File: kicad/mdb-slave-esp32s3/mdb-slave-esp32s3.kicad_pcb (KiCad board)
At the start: 2 copper layers, 39 x 40 mm, 45 parts, among them J1 MDB_Connector, J2 USB_C_Receptacle_USB2.0_16P, J3 Conn_01x03_Pin, J8 Conn_01x04_Pin, Q7 MMBT3904, SW1 SW_Push, U1 TLP785, U3 ESP32-S3FH4R2, U4 TLP785, U5 LM2594HVM-3.3, Y1 Crystal_GND24

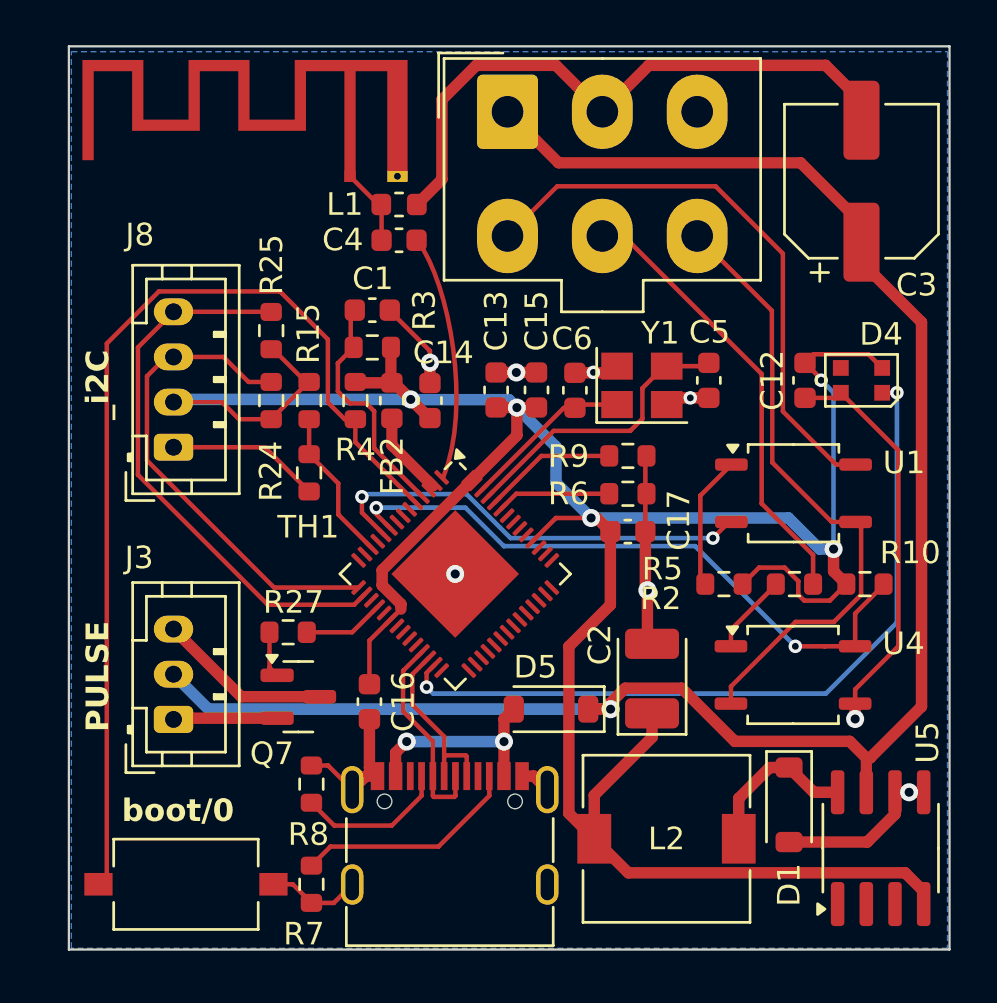
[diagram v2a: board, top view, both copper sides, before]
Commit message: small mounting hole
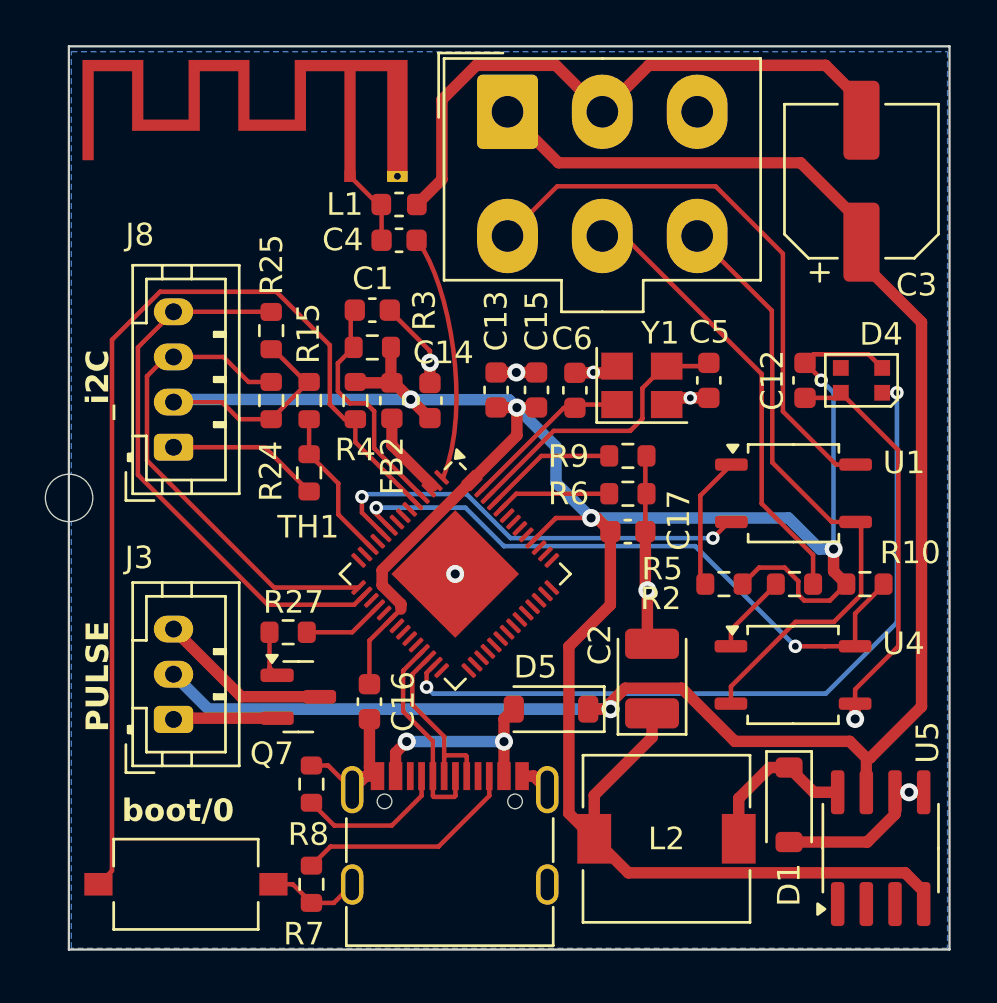
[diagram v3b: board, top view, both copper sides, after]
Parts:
- added H1: MountingHole, MountingHole:MountingHole_2.1mm, F.Cu at (168.5, 103.1)
- moved REF** 0.13 mm to (193.6, 107.4)

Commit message: routing pcb
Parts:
- moved C14 0.08 mm to (184.4, 98.8)
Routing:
- net GND: track 94.4 -> 82.0 mm, vias 8 -> 9
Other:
- board text added: "commit xxxxxxx"
- board text added: "i2C"
- board text removed: "_i2C"
- board text removed: "commit: xxxxxxx"

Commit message: routing...
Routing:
- net GND: track 82.0 -> 69.2 mm, vias 9 -> 10
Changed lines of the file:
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@@
 	(footprint "MountingHole:MountingHole_2.1mm"
 		(layer "F.Cu")
-		(at 168.51 103.09)
+		(at 168.5 103.09)
 		(descr "Mounting Hole 2.1mm, no annular, generated by kicad-footprint-generator mountinghole.py")
 		(tags "mountinghole")
@@
 	)
 	(segment
-		(start 185.02 88.9875)
-		(end 185.02 85.45837)
-		(width 0.508)
-		(layer "F.Cu")
-		(net 3)
-	)
-	(segment
 		(start 195.27 98.66)
 		(end 194.975 98.955)
@@
 	)
 	(segment
-		(start 185.02 85.45837)
-		(end 186.54577 83.9326)
-		(width 0.508)
-		(layer "F.Cu")
-		(net 3)
-	)
-	(segment
 		(start 202.46 98.66)
 		(end 202.685 98.435)
@@
 	)
 	(segment
+		(start 183.91 90.0975)
+		(end 184.79 90.0975)
+		(width 0.508)
+		(layer "F.Cu")
+		(net 3)
+	)
+	(segment
 		(start 205.085 117.099999)
 		(end 205.085 116.125)
@@
 	)
 	(segment
-		(start 190.0676 83.9326)
-		(end 192.125 85.99)
-		(width 0.508)
-		(layer "F.Cu")
-		(net 3)
-	)
-	(segment
 		(start 180.234 121.025)
 		(end 181.049 120.21)
@@
 	)
 	(segment
-		(start 186.54577 83.9326)
-		(end 190.0676 83.9326)
-		(width 0.508)
-		(layer "F.Cu")
-		(net 3)
-	)
-	(segment
 		(start 203.854999 118.33)
 		(end 205.085 117.099999)
@@
 	)
 	(segment
-		(start 183.91 90.0975)
-		(end 185.02 88.9875)
-		(width 0.508)
-		(layer "F.Cu")
-		(net 3)
-	)
-	(segment
 		(start 194.17 104.72)
 		(end 194.03 104.58)
@@
 		(net 3)
 	)
+	(via
+		(at 184.79 90.0975)
+		(size 0.8)
+		(drill 0.4)
+		(layers "F.Cu" "B.Cu")
+		(free yes)
+		(net 3)
+	)
 	(segment
 		(start 196.695 97.255)
@@
 	)
 	(segment
-		(start 173.135 110.898333)
-		(end 174.681667 112.445)
+		(start 183.925 112.445)
+		(end 192.49 112.445)
 		(width 0.508)
 		(layer "B.Cu")
@@
 	)
 	(segment
-		(start 174.681667 112.445)
-		(end 192.49 112.445)
+		(start 182.378333 110.898333)
+		(end 183.925 112.445)
+		(width 0.508)
+		(layer "B.Cu")
+		(net 7)
+	)
+	(segment
+		(start 173.135 110.898333)
+		(end 182.378333 110.898333)
 		(width 0.508)
 		(layer "B.Cu")
@@
 	(segment
 		(start 197.84 104.72)
-		(end 187.764308 104.72)
+		(end 190.9 104.72)
 		(width 0.2032)
 		(layer "B.Cu")
@@
 	)
 	(segment
-		(start 187.764308 104.72)
-		(end 186.012953 102.968645)
+		(start 190.9 104.72)
+		(end 189.148645 102.968645)
 		(width 0.2032)
 		(layer "B.Cu")
@@
 	)
 	(segment
-		(start 186.012953 102.968645)
+		(start 189.148645 102.968645)
 		(end 181.546914 102.968645)
 		(width 0.2032)
@@
 	)
 	(segment
-		(start 182.113272 103.523645)
-		(end 186.063645 103.523645)
+		(start 190.735 105.225)
+		(end 196.235 105.225)
 		(width 0.2032)
 		(layer "B.Cu")
@@
 	)
 	(segment
-		(start 187.765 105.225)
-		(end 196.235 105.225)
+		(start 196.235 105.225)
+		(end 200.671738 109.661738)
 		(width 0.2032)
 		(layer "B.Cu")
@@
 	)
 	(segment
-		(start 196.235 105.225)
-		(end 200.671738 109.661738)
+		(start 189.033645 103.523645)
+		(end 190.735 105.225)
 		(width 0.2032)
 		(layer "B.Cu")
@@
 	)
 	(segment
-		(start 186.063645 103.523645)
-		(end 187.765 105.225)
+		(start 182.113272 103.523645)
+		(end 189.033645 103.523645)
 		(width 0.2032)
 		(layer "B.Cu")
@@
 		(name "$teardrop_padvia$")
 		(hatch none 0.1)
-		(priority 30010)
+		(priority 30009)
 		(attr
 			(teardrop
@@
 	)
 	(zone
-		(net 23)
-		(net_name "/io10")
+		(net 2)
+		(net_name "+3V3")
 		(layer "F.Cu")
 		(name "$teardrop_padvia$")
 		(hatch none 0.1)
-		(priority 30005)
+		(priority 30007)
 		(attr
 			(teardrop
@@
 		(polygon
 			(pts
-				(xy 171.92558 97.592999) (xy 172.067001 97.73442) (xy 173.327746 97.446667) (xy 173.135707 96.84596)
-				(xy 172.271529 96.729613)
+				(xy 174.598471 98.946667) (xy 174.598471 98.746667) (xy 173.743342 98.347785) (xy 173.134 98.846667)
+				(xy 173.743342 99.345549)
 			)
 		)
@@
 		(name "$teardrop_padvia$")
 		(hatch none 0.1)
-		(priority 30003)
+		(priority 30002)
 		(attr
 			(teardrop
@@
 	)
 	(zone
-		(net 23)
-		(net_name "/io10")
+		(net 12)
+		(net_name "/mdb_master_receive")
 		(layer "F.Cu")
 		(name "$teardrop_padvia$")
 		(hatch none 0.1)
-		(priority 30009)
+		(priority 30001)
 		(attr
 			(teardrop
@@
 		(polygon
 			(pts
-				(xy 174.598471 96.946667) (xy 174.598471 96.746667) (xy 173.743342 96.347785) (xy 173.134 96.846667)
-				(xy 173.743342 97.345549)
+				(xy 189.792438 89.763983) (xy 189.651017 89.622562) (xy 188.139088 89.861698) (xy 187.924293 91.490707)
+				(xy 189.275 91.554214)
 			)
 		)
@@
 		(name "$teardrop_padvia$")
 		(hatch none 0.1)
-		(priority 30000)
+		(priority 30013)
 		(attr
 			(teardrop
@@
 		(polygon
 			(pts
-				(xy 190.507878 84.013668) (xy 190.148668 84.372878) (xy 190.775 86.054213) (xy 192.125707 85.990707)
-				(xy 191.910911 84.361698)
+				(xy 180.192157 120.9234) (xy 180.192157 121.1266) (xy 180.872955 121.067877) (xy 181.05 120.21)
+				(xy 180.549 119.996303)
 			)
 		)
 	)
 	(zone
-		(net 72)
-		(net_name "Net-(J3-Pin_3)")
+		(net 3)
+		(net_name "GND")
 		(layer "F.Cu")
 		(name "$teardrop_padvia$")
 		(hatch none 0.1)
-		(priority 30004)
+		(priority 30005)
 		(attr
 			(teardrop
@@
 		(polygon
 			(pts
-				(xy 173.9106 110.033144) (xy 174.269811 109.673933) (xy 173.998471 108.913276) (xy 173.134293 108.897626)
-				(xy 172.886472 109.498333)
+				(xy 174.61 100.948267) (xy 174.61 100.745067) (xy 173.855671 100.265697) (xy 173.134 100.846667)
+				(xy 173.855671 101.427637)
 			)
 		)
@@
 		(name "$teardrop_padvia$")
 		(hatch none 0.1)
-		(priority 30012)
+		(priority 30010)
 		(attr
 			(teardrop
@@
 		(polygon
 			(pts
-				(xy 188.730421 115.156) (xy 188.730421 115.664) (xy 189.189 116.286434) (xy 189.69 116.01) (xy 189.287099 115.16838)
+				(xy 182.007579 115.664) (xy 182.007579 115.156) (xy 181.4509 115.16838) (xy 181.048 116.01) (xy 181.549 116.286434)
 			)
 		)
 	)
 	(zone
-		(net 3)
-		(net_name "GND")
+		(net 23)
+		(net_name "/io10")
 		(layer "F.Cu")
 		(name "$teardrop_padvia$")
 		(hatch none 0.1)
-		(priority 30011)
+		(priority 30004)
 		(attr
 			(teardrop
@@
 		(polygon
 			(pts
-				(xy 182.007579 115.664) (xy 182.007579 115.156) (xy 181.4509 115.16838) (xy 181.048 116.01) (xy 181.549 116.286434)
+				(xy 171.92558 97.592999) (xy 172.067001 97.73442) (xy 173.327746 97.446667) (xy 173.135707 96.84596)
+				(xy 172.271529 96.729613)
 			)
 		)
@@
 		(name "$teardrop_padvia$")
 		(hatch none 0.1)
-		(priority 30007)
+		(priority 30006)
 		(attr
 			(teardrop
@@
 	)
 	(zone
-		(net 11)
-		(net_name "/mdb_communications_common")
-		(layer "F.Cu")
-		(name "$teardrop_padvia$")
-		(hatch none 0.1)
-		(priority 30001)
-		(attr
-			(teardrop
-				(type padvia)
-			)
-		)
-		(connect_pads yes
-			(clearance 0)
-		)
-		(min_thickness 0.0254)
-		(filled_areas_thickness no)
-		(fill yes
-			(thermal_gap 0.5)
-			(thermal_bridge_width 0.5)
-			(island_removal_mode 1)
-			(island_area_min 10)
-		)
-		(polygon
-			(pts
-				(xy 198.051017 93.357438) (xy 198.192438 93.216017) (xy 197.675 91.425786) (xy 196.324293 91.489293)
-				(xy 196.539087 93.118301)
-			)
-		)
-	)
-	(zone
 		(net 3)
 		(net_name "GND")
@@
 		(name "$teardrop_padvia$")
 		(hatch none 0.1)
-		(priority 30013)
+		(priority 30012)
 		(attr
 			(teardrop
@@
 	)
 	(zone
-		(net 2)
-		(net_name "+3V3")
+		(net 11)
+		(net_name "/mdb_communications_common")
 		(layer "F.Cu")
 		(name "$teardrop_padvia$")
 		(hatch none 0.1)
-		(priority 30008)
+		(priority 30000)
 		(attr
 			(teardrop
@@
 		(polygon
 			(pts
-				(xy 174.598471 98.946667) (xy 174.598471 98.746667) (xy 173.743342 98.347785) (xy 173.134 98.846667)
-				(xy 173.743342 99.345549)
+				(xy 198.051017 93.357438) (xy 198.192438 93.216017) (xy 197.675 91.425786) (xy 196.324293 91.489293)
+				(xy 196.539087 93.118301)
 			)
 		)
 	)
 	(zone
-		(net 3)
-		(net_name "GND")
+		(net 23)
+		(net_name "/io10")
 		(layer "F.Cu")
 		(name "$teardrop_padvia$")
 		(hatch none 0.1)
-		(priority 30006)
+		(priority 30008)
 		(attr
 			(teardrop
@@
 		(polygon
 			(pts
-				(xy 174.61 100.948267) (xy 174.61 100.745067) (xy 173.855671 100.265697) (xy 173.134 100.846667)
-				(xy 173.855671 101.427637)
+				(xy 174.598471 96.946667) (xy 174.598471 96.746667) (xy 173.743342 96.347785) (xy 173.134 96.846667)
+				(xy 173.743342 97.345549)
 			)
 		)
@@
 		(name "$teardrop_padvia$")
 		(hatch none 0.1)
-		(priority 30014)
+		(priority 30011)
 		(attr
 			(teardrop
@@
 		(polygon
 			(pts
-				(xy 180.192157 120.9234) (xy 180.192157 121.1266) (xy 180.872955 121.067877) (xy 181.05 120.21)
-				(xy 180.549 119.996303)
+				(xy 188.730421 115.156) (xy 188.730421 115.664) (xy 189.189 116.286434) (xy 189.69 116.01) (xy 189.287099 115.16838)
 			)
 		)
 	)
 	(zone
-		(net 12)
-		(net_name "/mdb_master_receive")
+		(net 72)
+		(net_name "Net-(J3-Pin_3)")
 		(layer "F.Cu")
 		(name "$teardrop_padvia$")
 		(hatch none 0.1)
-		(priority 30002)
+		(priority 30003)
 		(attr
 			(teardrop
@@
 		(polygon
 			(pts
-				(xy 189.792438 89.763983) (xy 189.651017 89.622562) (xy 188.139088 89.861698) (xy 187.924293 91.490707)
-				(xy 189.275 91.554214)
+				(xy 173.9106 110.033144) (xy 174.269811 109.673933) (xy 173.998471 108.913276) (xy 173.134293 108.897626)
+				(xy 172.886472 109.498333)
 			)
 		)
@@
 		(polygon
 			(pts
-				(xy 168.61 89.79) (xy 168.61 83.28) (xy 183.96 83.28) (xy 183.96 89.79)
+				(xy 168.61 89.62) (xy 168.61 83.28) (xy 183.96 83.28) (xy 183.96 89.62)
 			)
 		)
@@
 		(polygon
 			(pts
-				(xy 181.15 92.36) (xy 181.15 88.83) (xy 182.75 88.83) (xy 182.75 92.36)
+				(xy 181.54 92.36) (xy 181.54 88.83) (xy 183.14 88.83) (xy 183.14 92.36)
 			)
 		)
@@
 			(thermal_gap 0.5)
 			(thermal_bridge_width 0.5)
-			(hatch_thickness 1)
-			(hatch_gap 1.5)
+			(hatch_thickness 3)
+			(hatch_gap 1)
 			(hatch_orientation 0)
 			(hatch_border_algorithm hatch_thickness)

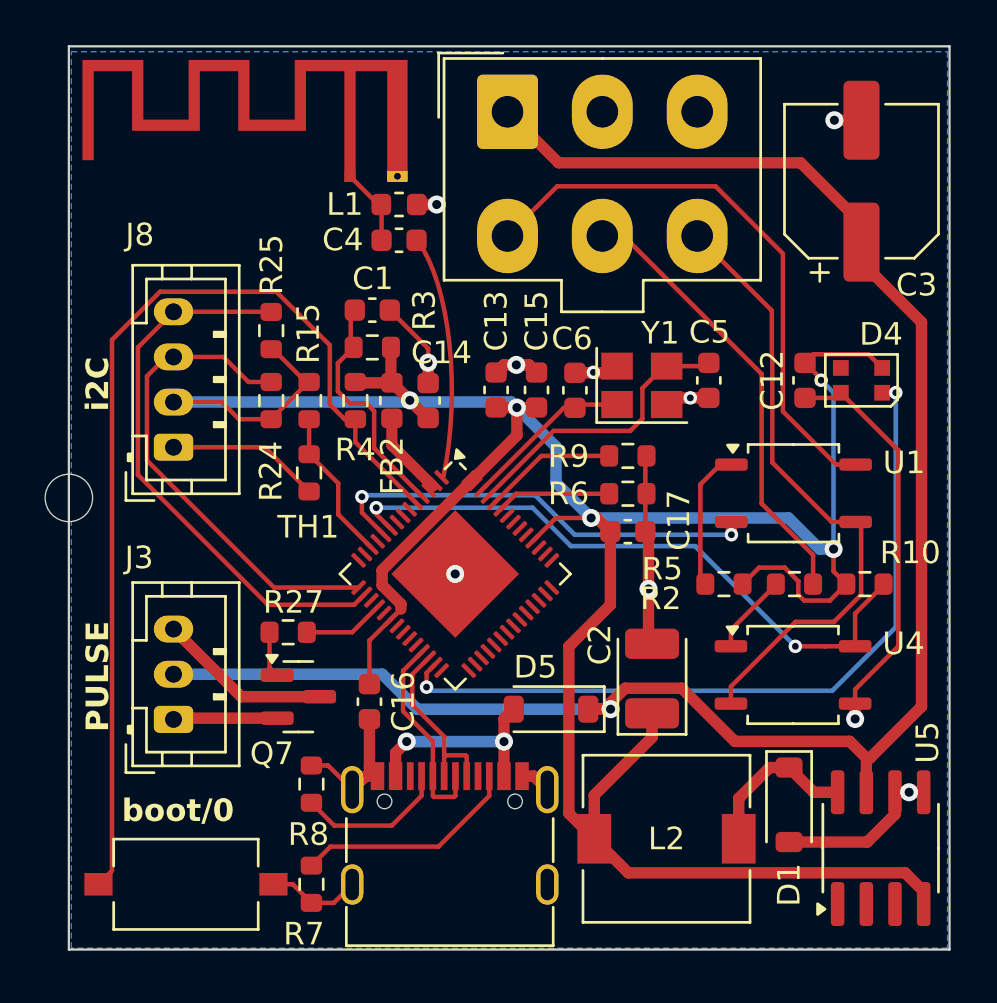
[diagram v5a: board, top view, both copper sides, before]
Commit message: moving capacitor 0.1uf to left ferrite bead
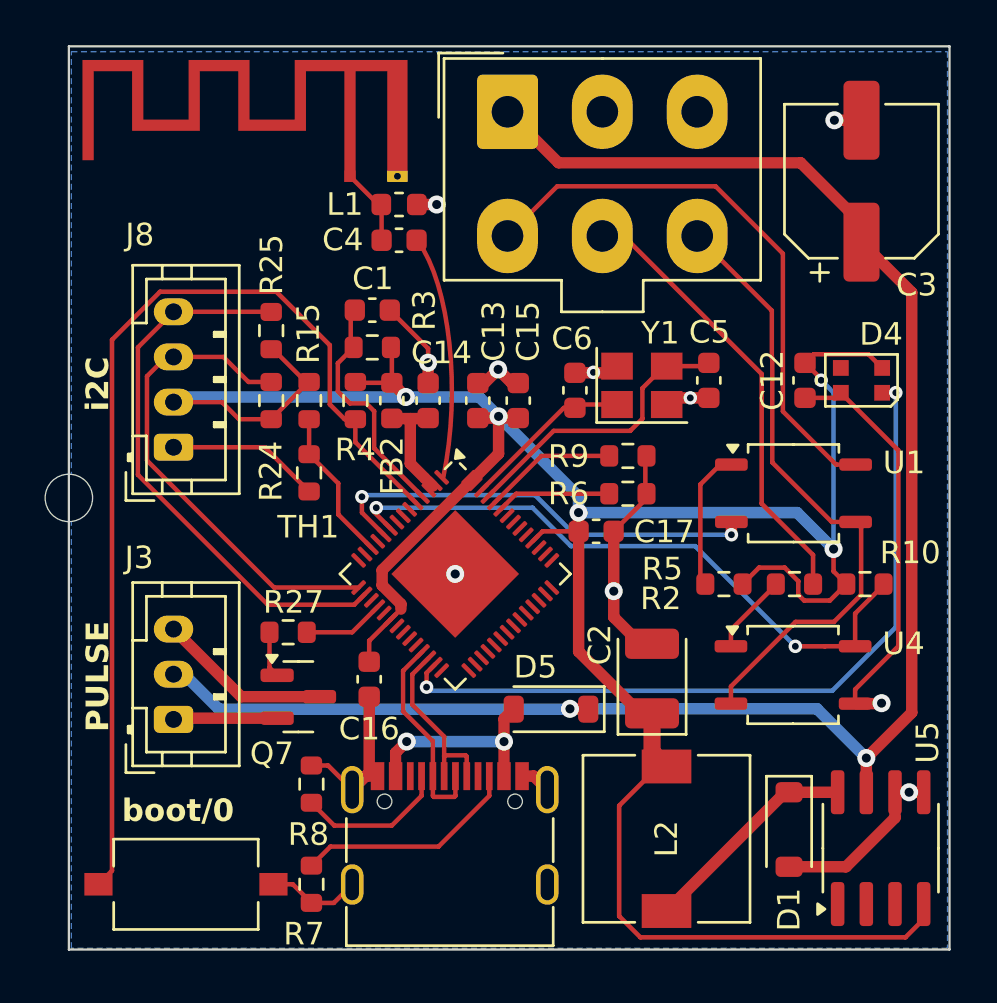
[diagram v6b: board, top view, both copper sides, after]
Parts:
- removed REF**: OSHW-Logo_11.4x12mm_SilkScreen, Symbol:OSHW-Logo_11.4x12mm_SilkScreen
- moved C17 1.41 mm to (191.8, 104.6)
- moved D1 1.09 mm to (200.4, 117.8)
- moved C16 1.00 mm to (181.8, 111.1)
- moved C15 0.94 mm to (188.4, 98.8)
- moved C13 0.94 mm to (186.6, 98.8)
- turned L2 to 90 degrees
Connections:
- C14 pad 2: +3V3 -> VDD3P3
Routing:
- net +3V3: track 127.4 -> 120.2 mm
- net GND: track 69.2 -> 72.8 mm
- net Net-(D1-K): track 7.19 -> 9.76 mm
- net /vin: track 79.3 -> 77.8 mm, vias 1 -> 2
- net VDD3P3: track 3.75 -> 5.07 mm

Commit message: adding open logo
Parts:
- added REF**: OSHW-Logo_11.4x12mm_SilkScreen, Symbol:OSHW-Logo_11.4x12mm_SilkScreen, B.Cu at (193.6, 107.5)
